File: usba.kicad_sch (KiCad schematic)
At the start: 9 parts, among them U10 XXL1509-5.0, U11 XXL1509-5.0, U8 RH792A, U9 XDUF-0426-081_C18202150

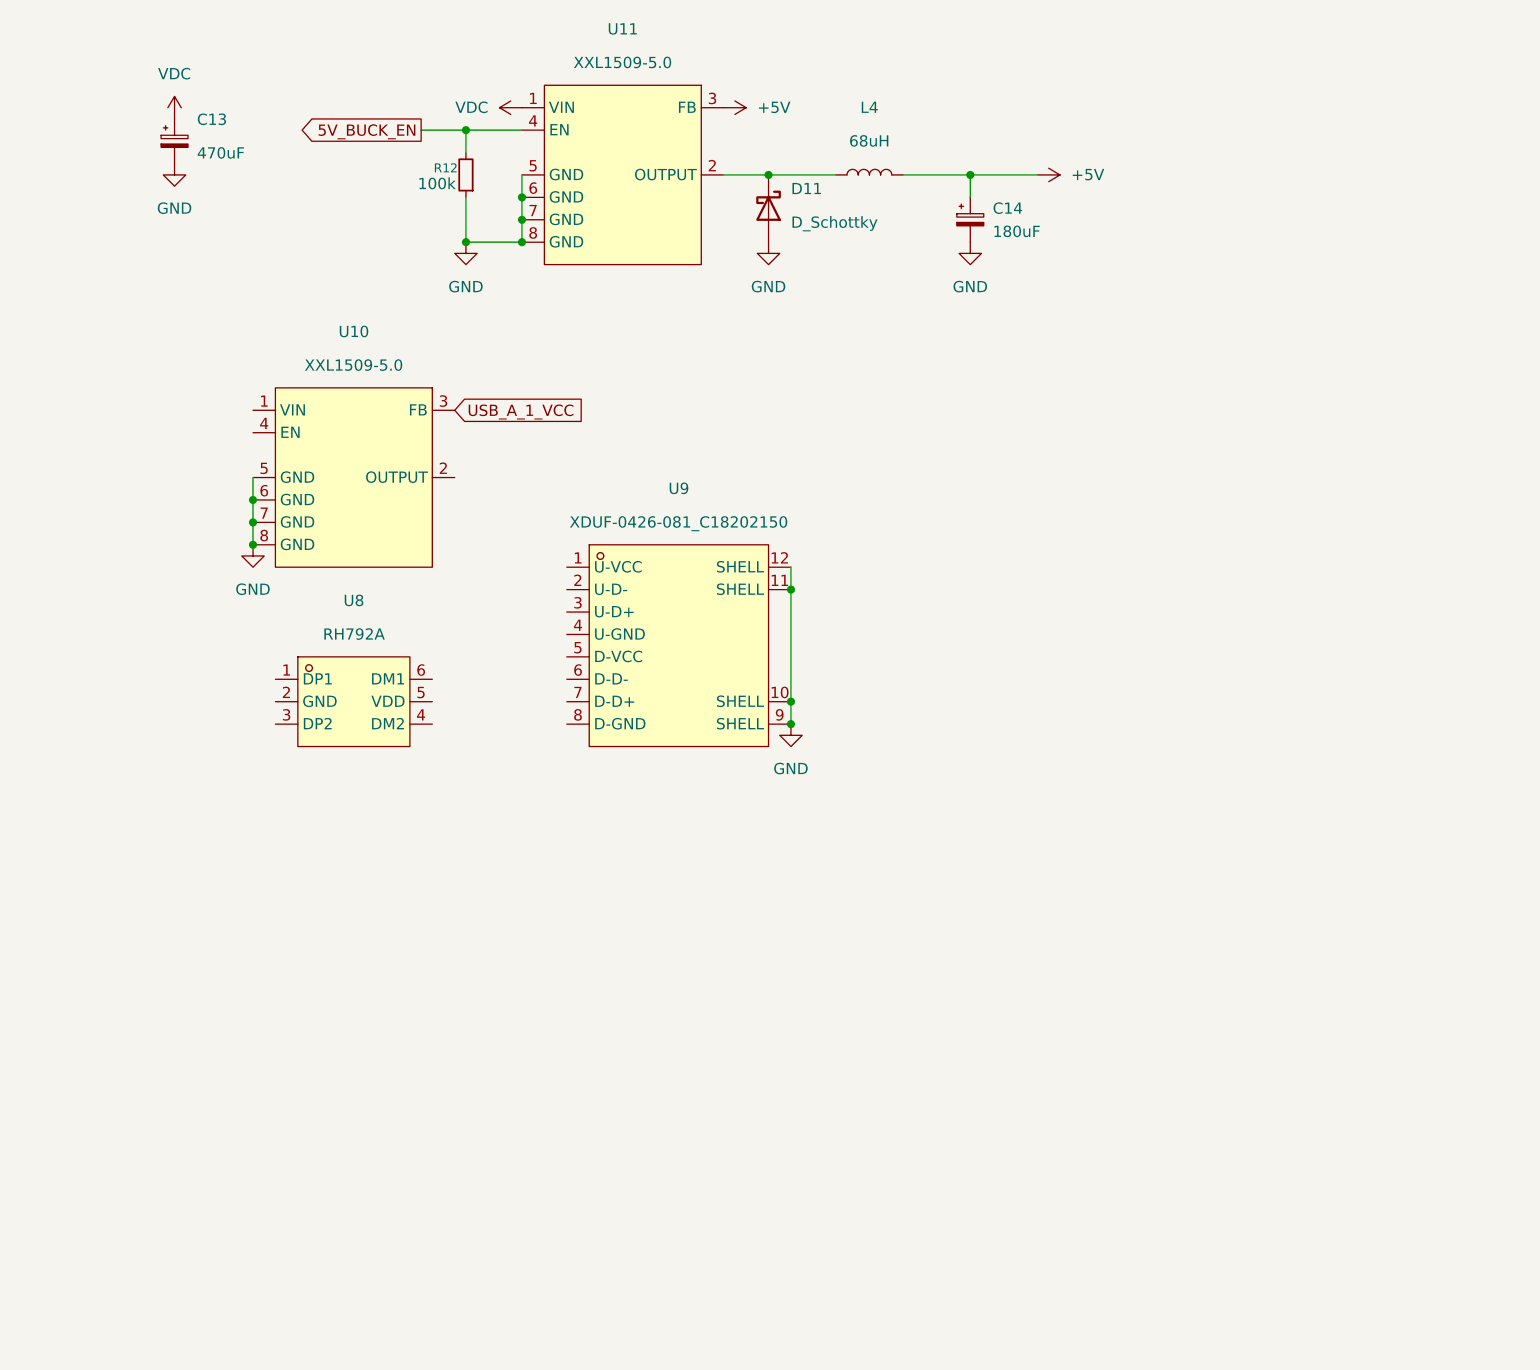
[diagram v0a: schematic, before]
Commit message: gave up on single board, gonna make small modules
Signed-off-by: Toby Cm <toby@vsus.app>
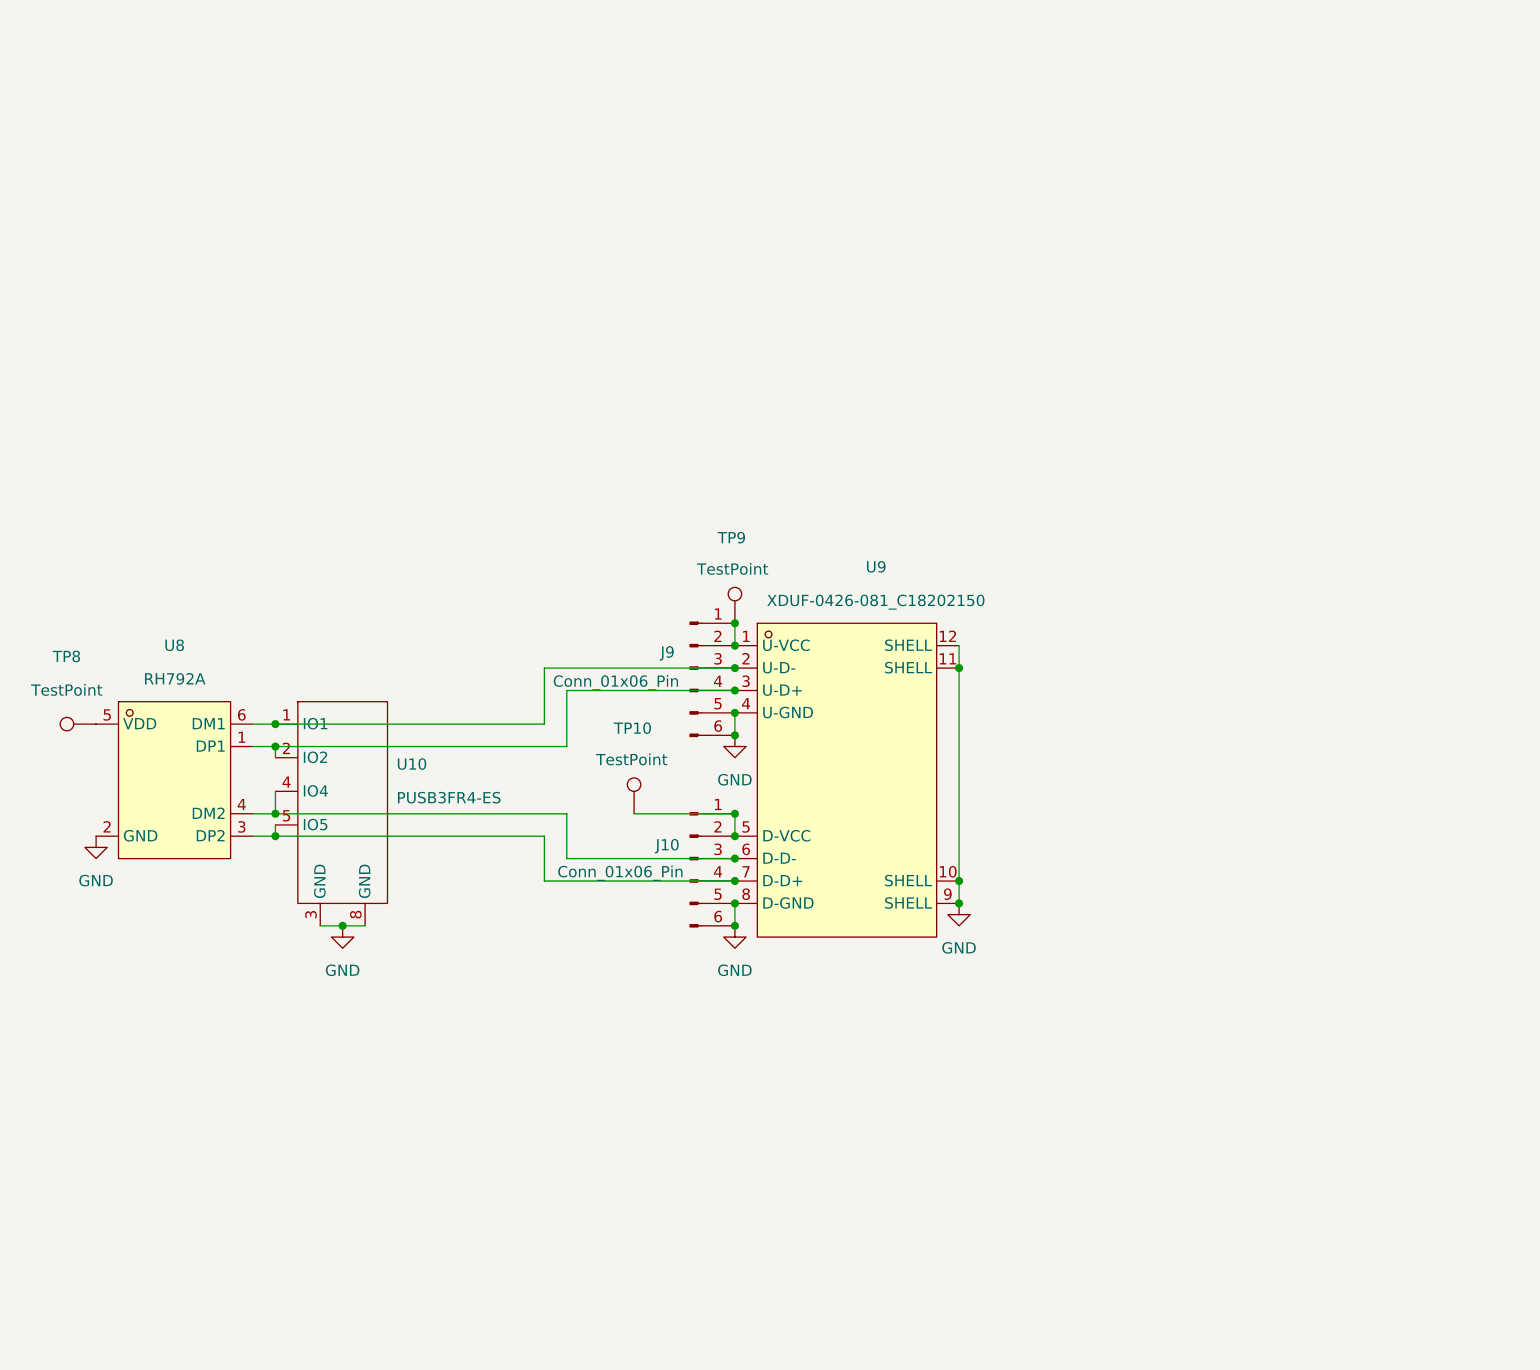
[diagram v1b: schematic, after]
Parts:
- removed C13: 470uF, symbol Device:C_Polarized_Small
- removed C14: 180uF, symbol Device:C_Polarized_Small
- removed D11: D_Schottky, symbol Device:D_Schottky
- removed L4: 68uH, symbol Device:L
- removed R12: 100k, symbol Device:R_Small
- removed U10, U11: XXL1509-5.0, easyeda2kicad:SOIC-8_L4.9-W3.9-P1.27-LS6.0-BL, symbol EasyEDA:XXL1509-5.0
- added J10, J9: Conn_01x06_Pin, Connector_PinHeader_2.54mm:PinHeader_1x06_P2.54mm_Vertical, symbol Connector:Conn_01x06_Pin
- added TP10, TP8, TP9: TestPoint, TestPoint:TestPoint_Pad_D2.0mm, symbol Connector:TestPoint
- added U10: PUSB3FR4-ES, Package_DFN_QFN:Diodes_UDFN-10_1.0x2.5mm_P0.5mm, symbol ElecSuper:PUSB3FR4-ES
- U8: symbol EasyEDA:RH792A -> easyeda2kicad:RH792A
- U9: symbol EasyEDA:XDUF-0426-081_C18202150 -> easyeda2kicad:XDUF-0426-081_C18202150
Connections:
- net GND: now also U8.2 (GND), U9.4 (U-GND), U9.8 (D-GND), J10.5 (Pin_5), J10.6 (Pin_6), J9.5 (Pin_5), J9.6 (Pin_6), U10.3 (GND), U10.8 (GND)
- net at U8.1 (DP1): now also U9.3 (U-D+), J9.4 (Pin_4), U10.2 (IO2)
- net at U8.3 (DP2): now also U9.7 (D-D+), J10.4 (Pin_4), U10.5 (IO5)
- net at U8.4 (DM2): now also U9.6 (D-D-), J10.3 (Pin_3), U10.4 (IO4)
- net at U8.5 (VDD): now also TP8.1
- net at U8.6 (DM1): now also U9.2 (U-D-), J9.3 (Pin_3), U10.1 (IO1)
- net at U9.1 (U-VCC): now also J9.1 (Pin_1), J9.2 (Pin_2), TP9.1
- net at U9.5 (D-VCC): now also J10.1 (Pin_1), J10.2 (Pin_2), TP10.1
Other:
- moved on the sheet: U8, U9

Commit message: updated journal, pin headers footprint, etc. added labels to rp2350b, finished pcb routing. time to start on other modules yay
Signed-off-by: Toby Cm <toby@vsus.app>
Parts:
- renumbered J9 to J8, J10 to J9, TP9 to TP1, TP8 to TP2, TP10 to TP3, U10 to U4, U9 to U5, U8 to U6
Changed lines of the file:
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@@
 		(dnp no)
 		(fields_autoplaced yes)
-		(property "Reference" "#PWR0112"
+		(property "Reference" "#PWR045"
 			(at 27.94 82.55 0)
 			(effects
@@
 			(project ""
 				(path "/04e54dfe-f06f-40ed-b860-573373578cb0/6cd18a35-eac9-4d54-ab2a-e3d56b6afb11"
-					(reference "#PWR0112")
+					(reference "#PWR045")
 					(unit 1)
 				)
@@
 		(on_board yes)
 		(dnp no)
-		(property "Reference" "TP10"
+		(property "Reference" "TP3"
 			(at 90.932 64.008 0)
 			(effects
@@
 			(project "usb-charging-hub"
 				(path "/04e54dfe-f06f-40ed-b860-573373578cb0/6cd18a35-eac9-4d54-ab2a-e3d56b6afb11"
-					(reference "TP10")
+					(reference "TP3")
 					(unit 1)
 				)
@@
 		(on_board yes)
 		(dnp no)
-		(property "Reference" "U8"
+		(property "Reference" "U6"
 			(at 36.83 54.61 0)
 			(effects
@@
 			(project "usb-charging-hub"
 				(path "/04e54dfe-f06f-40ed-b860-573373578cb0/6cd18a35-eac9-4d54-ab2a-e3d56b6afb11"
-					(reference "U8")
+					(reference "U6")
 					(unit 1)
 				)
@@
 		(on_board yes)
 		(dnp no)
-		(property "Reference" "J9"
+		(property "Reference" "J8"
 			(at 92.71 55.372 0)
 			(effects
@@
 			(project ""
 				(path "/04e54dfe-f06f-40ed-b860-573373578cb0/6cd18a35-eac9-4d54-ab2a-e3d56b6afb11"
-					(reference "J9")
+					(reference "J8")
 					(unit 1)
 				)
@@
 		(dnp no)
 		(fields_autoplaced yes)
-		(property "Reference" "TP8"
+		(property "Reference" "TP2"
 			(at 24.638 55.88 90)
 			(effects
@@
 			(project ""
 				(path "/04e54dfe-f06f-40ed-b860-573373578cb0/6cd18a35-eac9-4d54-ab2a-e3d56b6afb11"
-					(reference "TP8")
+					(reference "TP2")
 					(unit 1)
 				)
@@
 		(on_board yes)
 		(dnp no)
-		(property "Reference" "U9"
+		(property "Reference" "U5"
 			(at 116.332 45.72 0)
 			(effects
@@
 			(project "usb-charging-hub"
 				(path "/04e54dfe-f06f-40ed-b860-573373578cb0/6cd18a35-eac9-4d54-ab2a-e3d56b6afb11"
-					(reference "U9")
+					(reference "U5")
 					(unit 1)
 				)
@@
 		(dnp no)
 		(fields_autoplaced yes)
-		(property "Reference" "#PWR0115"
+		(property "Reference" "#PWR044"
 			(at 100.33 71.12 0)
 			(effects
@@
 			(project "usb-charging-hub"
 				(path "/04e54dfe-f06f-40ed-b860-573373578cb0/6cd18a35-eac9-4d54-ab2a-e3d56b6afb11"
-					(reference "#PWR0115")
+					(reference "#PWR044")
 					(unit 1)
 				)
@@
 		(dnp no)
 		(fields_autoplaced yes)
-		(property "Reference" "#PWR0113"
+		(property "Reference" "#PWR046"
 			(at 125.73 90.17 0)
 			(effects
@@
 			(project "usb-charging-hub"
 				(path "/04e54dfe-f06f-40ed-b860-573373578cb0/6cd18a35-eac9-4d54-ab2a-e3d56b6afb11"
-					(reference "#PWR0113")
+					(reference "#PWR046")
 					(unit 1)
 				)
@@
 		(dnp no)
 		(fields_autoplaced yes)
-		(property "Reference" "#PWR0116"
+		(property "Reference" "#PWR047"
 			(at 55.88 92.71 0)
 			(effects
@@
 			(project "usb-charging-hub"
 				(path "/04e54dfe-f06f-40ed-b860-573373578cb0/6cd18a35-eac9-4d54-ab2a-e3d56b6afb11"
-					(reference "#PWR0116")
+					(reference "#PWR047")
 					(unit 1)
 				)
@@
 		(on_board yes)
 		(dnp no)
-		(property "Reference" "TP9"
+		(property "Reference" "TP1"
 			(at 101.6 42.418 0)
 			(effects
@@
 			(project "usb-charging-hub"
 				(path "/04e54dfe-f06f-40ed-b860-573373578cb0/6cd18a35-eac9-4d54-ab2a-e3d56b6afb11"
-					(reference "TP9")
+					(reference "TP1")
 					(unit 1)
 				)
@@
 		(on_board yes)
 		(dnp no)
-		(property "Reference" "U10"
+		(property "Reference" "U4"
 			(at 61.976 68.072 0)
 			(effects
@@
 			(project ""
 				(path "/04e54dfe-f06f-40ed-b860-573373578cb0/6cd18a35-eac9-4d54-ab2a-e3d56b6afb11"
-					(reference "U10")
+					(reference "U4")
 					(unit 1)
 				)
@@
 		(dnp no)
 		(fields_autoplaced yes)
-		(property "Reference" "#PWR0114"
+		(property "Reference" "#PWR048"
 			(at 100.33 92.71 0)
 			(effects
@@
 			(project "usb-charging-hub"
 				(path "/04e54dfe-f06f-40ed-b860-573373578cb0/6cd18a35-eac9-4d54-ab2a-e3d56b6afb11"
-					(reference "#PWR0114")
+					(reference "#PWR048")
 					(unit 1)
 				)
@@
 		(on_board yes)
 		(dnp no)
-		(property "Reference" "J10"
+		(property "Reference" "J9"
 			(at 92.71 77.216 0)
 			(effects
@@
 			(project "usb-charging-hub"
 				(path "/04e54dfe-f06f-40ed-b860-573373578cb0/6cd18a35-eac9-4d54-ab2a-e3d56b6afb11"
-					(reference "J10")
-					(unit 1)
-				)
+					(reference "J9")
+					(unit 1)
+				)

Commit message: no more modules, its gonna work first try :fire: i love infineon and their ICs so much
Signed-off-by: Toby Cm <toby@vsus.app>
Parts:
- removed TP2: TestPoint, TestPoint:TestPoint_Pad_D2.0mm, symbol Connector:TestPoint
- removed U4: PUSB3FR4-ES, Package_DFN_QFN:Diodes_UDFN-10_1.0x2.5mm_P0.5mm, symbol ElecSuper:PUSB3FR4-ES
- removed U6: RH792A, easyeda2kicad:SOT-23-6_L2.9-W1.6-P0.95-LS2.9-BL, symbol easyeda2kicad:RH792A
- added U2: CYPD3175-24LQXQ, Package_DFN_QFN:QFN-24-1EP_4x4mm_P0.5mm_EP2.75x2.75mm, symbol Interface_USB:CYPD3175-24LQXQ
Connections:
- net GND: now also U2.22 (GND), U2.25 (GND)
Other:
- moved on the sheet: J8, J9, TP1, TP3, U5
